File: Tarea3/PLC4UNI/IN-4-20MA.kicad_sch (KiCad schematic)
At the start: 0 parts

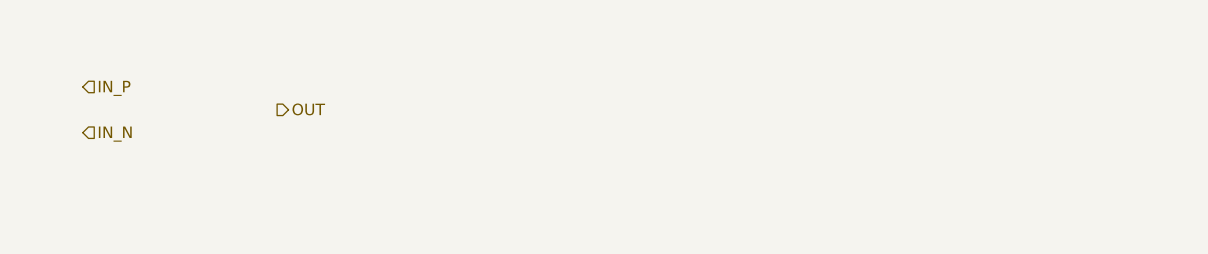
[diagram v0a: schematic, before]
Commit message: Cambio de directorio [Tarea2->CAD]
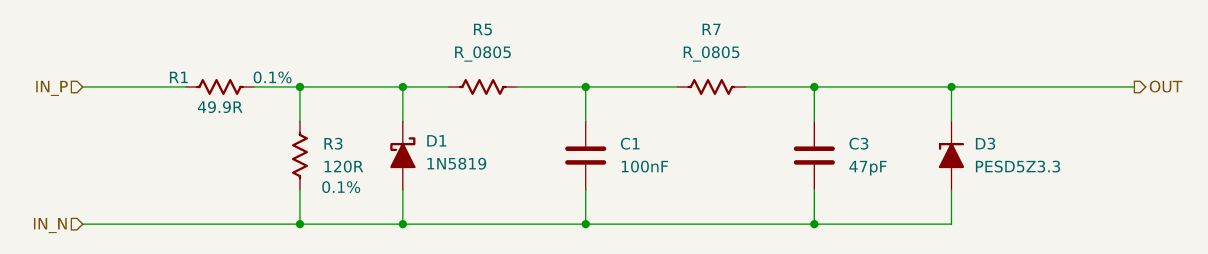
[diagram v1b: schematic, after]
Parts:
- added C1: 100nF, PCM_Capacitor_SMD_AKL:C_0603_1608Metric, symbol PCM_Capacitor_US_AKL:C_0603
- added C3: 47pF, PCM_Capacitor_SMD_AKL:C_0603_1608Metric, symbol PCM_Capacitor_US_AKL:C_0603
- added D1: 1N5819, PCM_Diode_THT_AKL:D_DO-41_SOD81_P7.62mm_Horizontal, symbol PCM_Diode_Schottky_AKL:1N5819
- added D3: PESD5Z3.3, PCM_Diode_SMD_AKL:D_SOD-523, symbol PCM_Diode_TVS_AKL:PESD5Z3.3
- added R1: 49.9R, PCM_Resistor_SMD_AKL:R_0805_2012Metric, symbol PCM_Resistor_US_AKL:R_0805
- added R3: 120R, PCM_Resistor_SMD_AKL:R_0805_2012Metric, symbol PCM_Resistor_US_AKL:R_0805
- added R5, R7: R_0805, PCM_Resistor_SMD_AKL:R_0805_2012Metric, symbol PCM_Resistor_US_AKL:R_0805
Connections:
- net IN_N: now also C1.2, C3.2, D1.2 (A), D3.2 (A), R3.1
- net IN_P: now also R1.1
- net OUT: now also C3.1, D3.1 (K), R7.2
- new net: C1.1, R5.2, R7.1
- new net: D1.1 (K), R1.2, R3.2, R5.1
